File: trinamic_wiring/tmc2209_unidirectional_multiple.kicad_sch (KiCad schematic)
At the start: 3 parts

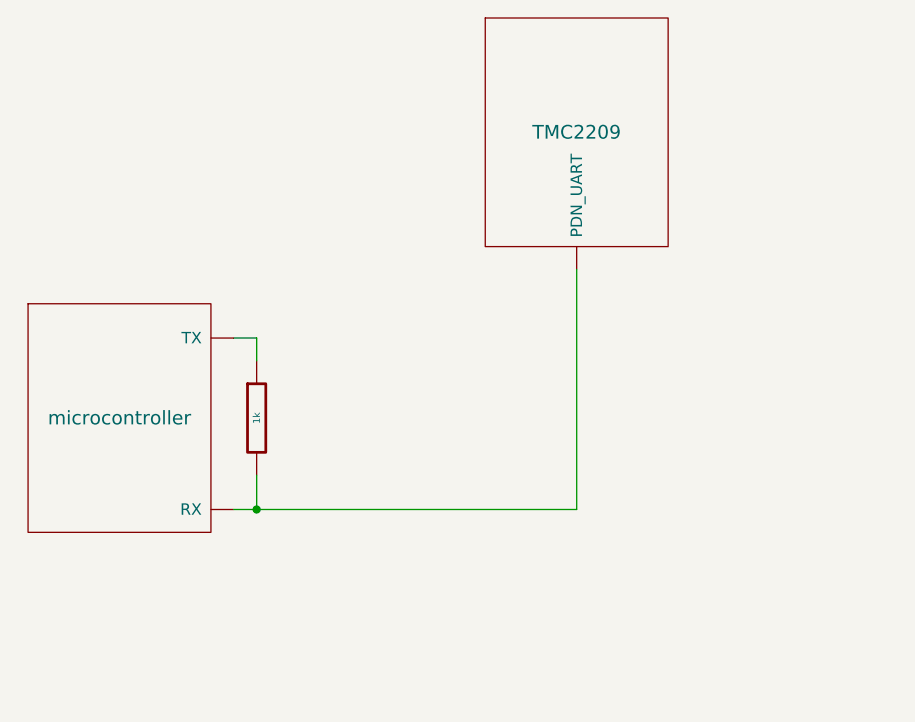
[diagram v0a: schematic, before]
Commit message: Add multiple chip schematics
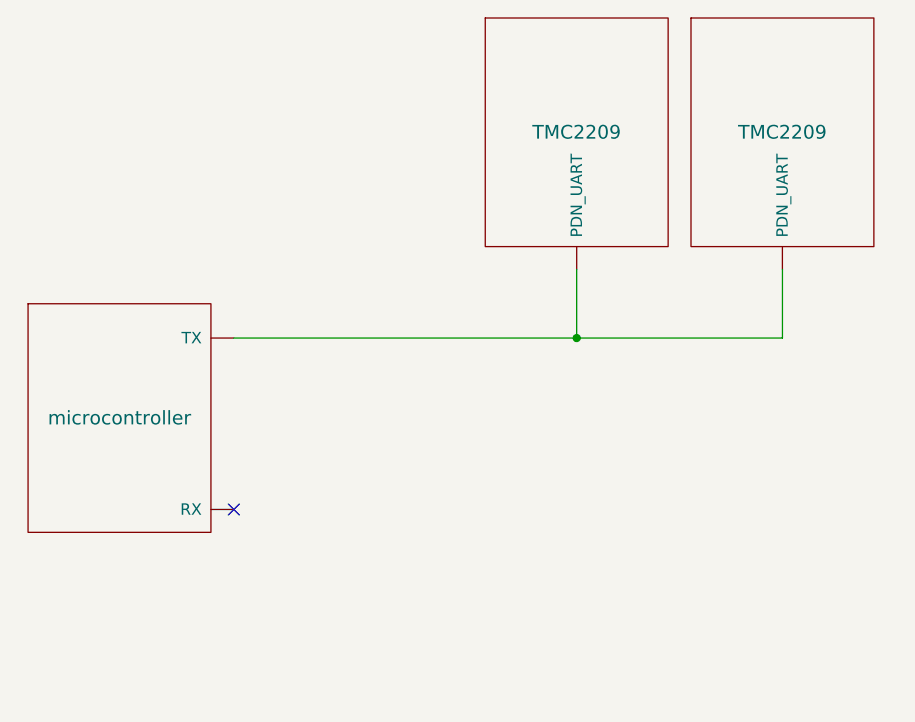
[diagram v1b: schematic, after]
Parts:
- removed R2: 1k, Janelia:R_0402_1005Metric, symbol Janelia:R_1k_0402
- added TMC?: TMC2209, symbol Janelia:SIMPLIFIED_TMC2209_UART
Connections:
- net at microcontroller?.0 (RX): no longer TMC?.0 (PDN_UART)
- net at microcontroller?.1 (TX): now also TMC?.0 (PDN_UART), TMC?.0 (PDN_UART)
- no-connect marks 0 -> 1
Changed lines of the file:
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@@
     (company "Janelia Research Campus")
   )
-  (junction (at 102.87 106.68) (diameter 0) (color 0 0 0 0)
+  (junction (at 138.43 87.63) (diameter 0) (color 0 0 0 0)
   )
-  (wire (pts (xy 102.87 87.63) (xy 102.87 90.17))
+  (no_connect (at 100.33 106.68))
+  (wire (pts (xy 138.43 87.63) (xy 161.29 87.63))
     (stroke (width 0) (type default))
   )
-  (wire (pts (xy 138.43 80.01) (xy 138.43 106.68))
+  (wire (pts (xy 138.43 80.01) (xy 138.43 87.63))
     (stroke (width 0) (type default))
   )
-  (wire (pts (xy 102.87 106.68) (xy 138.43 106.68))
+  (wire (pts (xy 100.33 87.63) (xy 138.43 87.63))
     (stroke (width 0) (type default))
   )
-  (wire (pts (xy 102.87 102.87) (xy 102.87 106.68))
-    (stroke (width 0) (type default))
-  )
-  (wire (pts (xy 100.33 87.63) (xy 102.87 87.63))
-    (stroke (width 0) (type default))
-  )
-  (wire (pts (xy 100.33 106.68) (xy 102.87 106.68))
+  (wire (pts (xy 161.29 80.01) (xy 161.29 87.63))
     (stroke (width 0) (type default))
   )
@@
           (reference "microcontroller1") (unit 1)
         )
-        (path "/e4144788-6304-493f-818e-5d881d3b7418/c8eda2b5-ab13-4033-82d9-875c9fcaf884/5f6f310d-167d-42a3-8815-1b623fe73dc8"
-          (reference "microcontroller2") (unit 1)
+        (path "/e4144788-6304-493f-818e-5d881d3b7418/c8eda2b5-ab13-4033-82d9-875c9fcaf884/5b0a2695-6b0b-4c82-b9d6-7e19fee75501"
+          (reference "microcontroller3") (unit 1)
+        )
+        (path "/e4144788-6304-493f-818e-5d881d3b7418/c8eda2b5-ab13-4033-82d9-875c9fcaf884/a2ce530e-f5b5-4e3e-9188-e4bc8f84c739"
+          (reference "microcontroller4") (unit 1)
         )
       )
@@
           (reference "TMC1") (unit 1)
         )
-        (path "/e4144788-6304-493f-818e-5d881d3b7418/c8eda2b5-ab13-4033-82d9-875c9fcaf884/5f6f310d-167d-42a3-8815-1b623fe73dc8"
-          (reference "TMC2") (unit 1)
+        (path "/e4144788-6304-493f-818e-5d881d3b7418/c8eda2b5-ab13-4033-82d9-875c9fcaf884/5b0a2695-6b0b-4c82-b9d6-7e19fee75501"
+          (reference "TMC4") (unit 1)
+        )
+        (path "/e4144788-6304-493f-818e-5d881d3b7418/c8eda2b5-ab13-4033-82d9-875c9fcaf884/a2ce530e-f5b5-4e3e-9188-e4bc8f84c739"
+          (reference "TMC6") (unit 1)
         )
       )
     )
   )
-  (symbol (lib_id "Janelia:R_1k_0402") (at 102.87 96.52 0) (unit 1)
-    (in_bom yes) (on_board yes) (dnp no)
-    (property "Reference" "R2" (at 104.14 96.52 0)
-      (effects (font (size 1.016 1.016)) (justify left) hide)
-    )
-    (property "Value" "1k" (at 102.87 96.52 90)
-      (effects (font (size 0.762 0.762)))
-    )
-    (property "Footprint" "Janelia:R_0402_1005Metric" (at 101.092 96.52 90)
-      (effects (font (size 0.762 0.762)) hide)
-    )
-    (property "Datasheet" "" (at 104.902 96.52 90)
-      (effects (font (size 0.762 0.762)))
-    )
-    (property "Vendor" "Digi-Key" (at 107.442 93.98 90)
+  (symbol (lib_id "Janelia:SIMPLIFIED_TMC2209_UART") (at 161.29 64.77 0) (unit 1)
+    (in_bom yes) (on_board yes) (dnp no) (fields_autoplaced)
+    (property "Reference" "TMC?" (at 161.29 64.77 0) (do_not_autoplace)
       (effects (font (size 1.524 1.524)) hide)
     )
-    (property "Vendor Part Number" "311-1.00KLRCT-ND" (at 109.982 91.44 90)
+    (property "Value" "TMC2209" (at 161.29 64.77 0)
+      (effects (font (size 1.524 1.524)))
+    )
+    (property "Footprint" "" (at 158.75 91.44 0)
       (effects (font (size 1.524 1.524)) hide)
     )
-    (property "Description" "RES SMD 1K OHM 1% 1/16W" (at 112.522 88.9 90)
+    (property "Datasheet" "" (at 161.29 64.77 0)
       (effects (font (size 1.524 1.524)) hide)
     )
-    (property "Package" "0402" (at 102.87 96.52 0)
-      (effects (font (size 1.27 1.27)) hide)
-    )
-    (property "Manufacturer" "YAGEO" (at 102.87 96.52 0)
-      (effects (font (size 1.27 1.27)) hide)
-    )
-    (property "Manufacturer Part Number" "RC0402FR-071KL" (at 102.87 96.52 0)
-      (effects (font (size 1.27 1.27)) hide)
-    )
-    (pin "1")
-    (pin "2")
+    (pin "0")
     (instances
       (project "trinamic_wiring"
+        (path "/e4144788-6304-493f-818e-5d881d3b7418/c8eda2b5-ab13-4033-82d9-875c9fcaf884/13e2a7b5-46df-44bb-8dde-5d79d190b8bf"
+          (reference "TMC?") (unit 1)
+        )
         (path "/e4144788-6304-493f-818e-5d881d3b7418/c8eda2b5-ab13-4033-82d9-875c9fcaf884/e3613d8e-f506-47d6-ad2d-b0f5798d9847"
-          (reference "R2") (unit 1)
+          (reference "TMC1") (unit 1)
         )
-        (path "/e4144788-6304-493f-818e-5d881d3b7418/c8eda2b5-ab13-4033-82d9-875c9fcaf884/5f6f310d-167d-42a3-8815-1b623fe73dc8"
-          (reference "R3") (unit 1)
+        (path "/e4144788-6304-493f-818e-5d881d3b7418/c8eda2b5-ab13-4033-82d9-875c9fcaf884/5b0a2695-6b0b-4c82-b9d6-7e19fee75501"
+          (reference "TMC5") (unit 1)
+        )
+        (path "/e4144788-6304-493f-818e-5d881d3b7418/c8eda2b5-ab13-4033-82d9-875c9fcaf884/a2ce530e-f5b5-4e3e-9188-e4bc8f84c739"
+          (reference "TMC7") (unit 1)
         )
       )

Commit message: Redo schematic symbols
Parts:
- removed TMC? (x2): TMC2209, symbol Janelia:SIMPLIFIED_TMC2209_UART
- removed microcontroller?: microcontroller, symbol Janelia:SIMPLIFIED_MCU_UART
- added MICROCONTROLLER4: DOC_MCU_UART, symbol Janelia:DOC_MCU_UART
- added TMC6 (x2): DOC_TMC2209, symbol Janelia:DOC_TMC2209
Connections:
- new net: MICROCONTROLLER4.1 (TX), TMC6.0 (UART), TMC6.0 (UART)
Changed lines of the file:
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@@
     (company "Janelia Research Campus")
   )
-  (junction (at 138.43 87.63) (diameter 0) (color 0 0 0 0)
+  (junction (at 148.59 77.47) (diameter 0) (color 0 0 0 0)
   )
-  (no_connect (at 100.33 106.68))
-  (wire (pts (xy 138.43 87.63) (xy 161.29 87.63))
+  (no_connect (at 125.73 97.79))
+  (wire (pts (xy 148.59 77.47) (xy 151.13 77.47))
     (stroke (width 0) (type default))
   )
-  (wire (pts (xy 138.43 80.01) (xy 138.43 87.63))
+  (wire (pts (xy 148.59 77.47) (xy 148.59 105.41))
     (stroke (width 0) (type default))
   )
-  (wire (pts (xy 100.33 87.63) (xy 138.43 87.63))
+  (wire (pts (xy 125.73 77.47) (xy 148.59 77.47))
     (stroke (width 0) (type default))
   )
-  (wire (pts (xy 161.29 80.01) (xy 161.29 87.63))
+  (wire (pts (xy 148.59 105.41) (xy 151.13 105.41))
     (stroke (width 0) (type default))
   )
-  (symbol (lib_id "Janelia:SIMPLIFIED_MCU_UART") (at 87.63 96.52 0) (unit 1)
-    (in_bom yes) (on_board yes) (dnp no)
-    (property "Reference" "microcontroller?" (at 87.63 96.52 0) (do_not_autoplace)
+  (symbol (lib_id "Janelia:DOC_MCU_UART") (at 113.03 87.63 0) (unit 1)
+    (in_bom yes) (on_board yes) (dnp no) (fields_autoplaced)
+    (property "Reference" "MICROCONTROLLER4" (at 113.03 68.58 0) (do_not_autoplace)
+      (effects (font (size 1.27 1.27)) hide)
+    )
+    (property "Value" "DOC_MCU_UART" (at 113.03 73.66 0)
       (effects (font (size 1.524 1.524)) hide)
     )
-    (property "Value" "microcontroller" (at 87.63 96.52 0)
-      (effects (font (size 1.524 1.524)))
-    )
-    (property "Footprint" "" (at 85.09 123.19 0)
+    (property "Footprint" "" (at 110.49 114.3 0)
       (effects (font (size 1.524 1.524)) hide)
     )
-    (property "Datasheet" "" (at 87.63 96.52 0)
+    (property "Datasheet" "" (at 113.03 87.63 0)
       (effects (font (size 1.524 1.524)) hide)
+    )
+    (property "Sim.Enable" "0" (at 113.03 71.12 0)
+      (effects (font (size 1.27 1.27)) hide)
     )
     (pin "0")
@@
       (project "trinamic_wiring"
         (path "/e4144788-6304-493f-818e-5d881d3b7418/c8eda2b5-ab13-4033-82d9-875c9fcaf884/13e2a7b5-46df-44bb-8dde-5d79d190b8bf"
-          (reference "microcontroller?") (unit 1)
-        )
-        (path "/e4144788-6304-493f-818e-5d881d3b7418/c8eda2b5-ab13-4033-82d9-875c9fcaf884/e3613d8e-f506-47d6-ad2d-b0f5798d9847"
-          (reference "microcontroller1") (unit 1)
+          (reference "MICROCONTROLLER4") (unit 1)
         )
         (path "/e4144788-6304-493f-818e-5d881d3b7418/c8eda2b5-ab13-4033-82d9-875c9fcaf884/5b0a2695-6b0b-4c82-b9d6-7e19fee75501"
-          (reference "microcontroller3") (unit 1)
-        )
-        (path "/e4144788-6304-493f-818e-5d881d3b7418/c8eda2b5-ab13-4033-82d9-875c9fcaf884/a2ce530e-f5b5-4e3e-9188-e4bc8f84c739"
-          (reference "microcontroller4") (unit 1)
+          (reference "MICROCONTROLLER1") (unit 1)
         )
       )
     )
   )
-  (symbol (lib_id "Janelia:SIMPLIFIED_TMC2209_UART") (at 138.43 64.77 0) (unit 1)
+  (symbol (lib_id "Janelia:DOC_TMC2209") (at 163.83 87.63 0) (unit 1)
     (in_bom yes) (on_board yes) (dnp no) (fields_autoplaced)
-    (property "Reference" "TMC?" (at 138.43 64.77 0) (do_not_autoplace)
+    (property "Reference" "TMC6" (at 163.83 68.58 0)
+      (effects (font (size 1.27 1.27)) hide)
+    )
+    (property "Value" "DOC_TMC2209" (at 163.83 73.66 0)
       (effects (font (size 1.524 1.524)) hide)
     )
-    (property "Value" "TMC2209" (at 138.43 64.77 0)
-      (effects (font (size 1.524 1.524)))
-    )
-    (property "Footprint" "" (at 135.89 91.44 0)
+    (property "Footprint" "" (at 161.29 114.3 0)
       (effects (font (size 1.524 1.524)) hide)
     )
-    (property "Datasheet" "" (at 138.43 64.77 0)
+    (property "Datasheet" "" (at 163.83 87.63 0)
       (effects (font (size 1.524 1.524)) hide)
     )
+    (property "Sim.Enable" "0" (at 163.83 71.12 0)
+      (effects (font (size 1.27 1.27)) hide)
+    )
     (pin "0")
+    (pin "1")
+    (pin "10")
+    (pin "2")
+    (pin "3")
+    (pin "4")
+    (pin "5")
+    (pin "6")
+    (pin "7")
+    (pin "8")
+    (pin "9")
     (instances
       (project "trinamic_wiring"
         (path "/e4144788-6304-493f-818e-5d881d3b7418/c8eda2b5-ab13-4033-82d9-875c9fcaf884/13e2a7b5-46df-44bb-8dde-5d79d190b8bf"
-          (reference "TMC?") (unit 1)
-        )
-        (path "/e4144788-6304-493f-818e-5d881d3b7418/c8eda2b5-ab13-4033-82d9-875c9fcaf884/e3613d8e-f506-47d6-ad2d-b0f5798d9847"
-          (reference "TMC1") (unit 1)
+          (reference "TMC6") (unit 1)
         )
         (path "/e4144788-6304-493f-818e-5d881d3b7418/c8eda2b5-ab13-4033-82d9-875c9fcaf884/5b0a2695-6b0b-4c82-b9d6-7e19fee75501"
-          (reference "TMC4") (unit 1)
-        )
-        (path "/e4144788-6304-493f-818e-5d881d3b7418/c8eda2b5-ab13-4033-82d9-875c9fcaf884/a2ce530e-f5b5-4e3e-9188-e4bc8f84c739"
-          (reference "TMC6") (unit 1)
+          (reference "TMC1") (unit 1)
         )
       )
     )
   )
-  (symbol (lib_id "Janelia:SIMPLIFIED_TMC2209_UART") (at 161.29 64.77 0) (unit 1)
+  (symbol (lib_id "Janelia:DOC_TMC2209") (at 163.83 115.57 0) (unit 1)
     (in_bom yes) (on_board yes) (dnp no) (fields_autoplaced)
-    (property "Reference" "TMC?" (at 161.29 64.77 0) (do_not_autoplace)
+    (property "Reference" "TMC6" (at 163.83 96.52 0)
+      (effects (font (size 1.27 1.27)) hide)
+    )
+    (property "Value" "DOC_TMC2209" (at 163.83 101.6 0)
       (effects (font (size 1.524 1.524)) hide)
     )
-    (property "Value" "TMC2209" (at 161.29 64.77 0)
-      (effects (font (size 1.524 1.524)))
-    )
-    (property "Footprint" "" (at 158.75 91.44 0)
+    (property "Footprint" "" (at 161.29 142.24 0)
       (effects (font (size 1.524 1.524)) hide)
     )
-    (property "Datasheet" "" (at 161.29 64.77 0)
+    (property "Datasheet" "" (at 163.83 115.57 0)
       (effects (font (size 1.524 1.524)) hide)
     )
+    (property "Sim.Enable" "0" (at 163.83 99.06 0)
+      (effects (font (size 1.27 1.27)) hide)
+    )
     (pin "0")
+    (pin "1")
+    (pin "10")
+    (pin "2")
+    (pin "3")
+    (pin "4")
+    (pin "5")
+    (pin "6")
+    (pin "7")
+    (pin "8")
+    (pin "9")
     (instances
       (project "trinamic_wiring"
         (path "/e4144788-6304-493f-818e-5d881d3b7418/c8eda2b5-ab13-4033-82d9-875c9fcaf884/13e2a7b5-46df-44bb-8dde-5d79d190b8bf"
-          (reference "TMC?") (unit 1)
-        )
-        (path "/e4144788-6304-493f-818e-5d881d3b7418/c8eda2b5-ab13-4033-82d9-875c9fcaf884/e3613d8e-f506-47d6-ad2d-b0f5798d9847"
-          (reference "TMC1") (unit 1)
+          (reference "TMC6") (unit 1)
         )
         (path "/e4144788-6304-493f-818e-5d881d3b7418/c8eda2b5-ab13-4033-82d9-875c9fcaf884/5b0a2695-6b0b-4c82-b9d6-7e19fee75501"
-          (reference "TMC5") (unit 1)
-        )
-        (path "/e4144788-6304-493f-818e-5d881d3b7418/c8eda2b5-ab13-4033-82d9-875c9fcaf884/a2ce530e-f5b5-4e3e-9188-e4bc8f84c739"
-          (reference "TMC7") (unit 1)
+          (reference "TMC8") (unit 1)
         )
       )

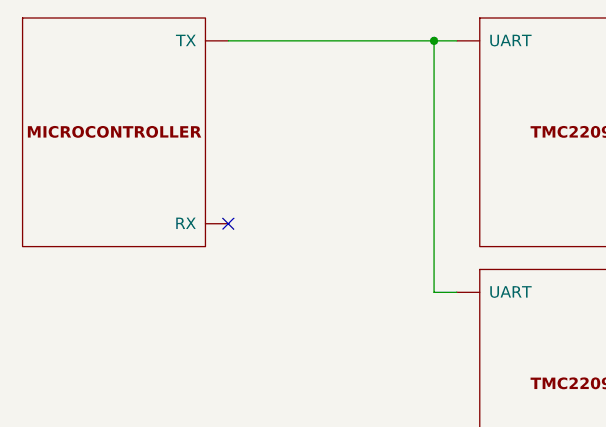
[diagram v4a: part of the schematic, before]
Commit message: Add more schematics
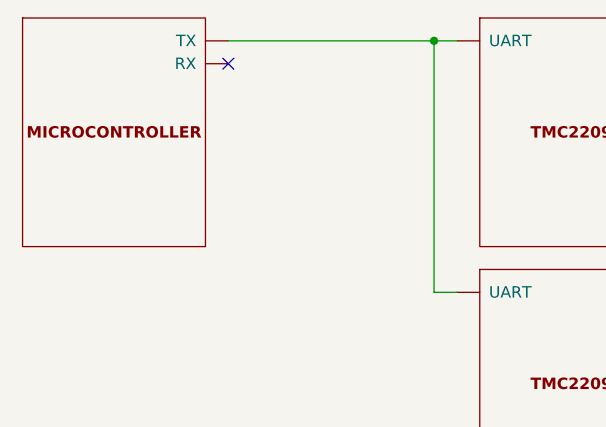
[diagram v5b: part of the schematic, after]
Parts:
- removed MICROCONTROLLER4: DOC_MCU_UART, symbol Janelia:DOC_MCU_UART
- added MICROCONTROLLER4: DOC_MCU, symbol Janelia:DOC_MCU
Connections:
- net at TMC6.0 (UART), TMC6.0 (UART): now also MICROCONTROLLER4.1 (TX)
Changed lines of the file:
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@@
   (title_block
     (title "Trinamic Wiring")
-    (date "2023-08-01")
+    (date "2023-08-02")
     (rev "0.4")
     (company "Janelia Research Campus")
@@
   (junction (at 148.59 77.47) (diameter 0) (color 0 0 0 0)
   )
-  (no_connect (at 125.73 97.79))
+  (no_connect (at 125.73 80.01))
   (wire (pts (xy 148.59 77.47) (xy 151.13 77.47))
     (stroke (width 0) (type default))
@@
     (stroke (width 0) (type default))
   )
-  (symbol (lib_id "Janelia:DOC_MCU_UART") (at 113.03 87.63 0) (unit 1)
+  (symbol (lib_id "Janelia:DOC_MCU") (at 113.03 87.63 0) (unit 1)
     (in_bom yes) (on_board yes) (dnp no) (fields_autoplaced)
-    (property "Reference" "MICROCONTROLLER4" (at 113.03 68.58 0) (do_not_autoplace)
+    (property "Reference" "MICROCONTROLLER4" (at 113.03 68.58 0)
       (effects (font (size 1.27 1.27)) hide)
     )
-    (property "Value" "DOC_MCU_UART" (at 113.03 73.66 0)
+    (property "Value" "DOC_MCU" (at 113.03 73.66 0)
       (effects (font (size 1.524 1.524)) hide)
     )
@@
     (pin "0")
     (pin "1")
+    (pin "2")
+    (pin "3")
+    (pin "4")
+    (pin "5")
+    (pin "6")
+    (pin "7")
+    (pin "8")
     (instances
       (project "trinamic_wiring"
@@
         (path "/e4144788-6304-493f-818e-5d881d3b7418/c8eda2b5-ab13-4033-82d9-875c9fcaf884/5b0a2695-6b0b-4c82-b9d6-7e19fee75501"
           (reference "MICROCONTROLLER1") (unit 1)
+        )
+        (path "/e4144788-6304-493f-818e-5d881d3b7418/c8eda2b5-ab13-4033-82d9-875c9fcaf884/d4a56977-1958-4e49-bd54-bb12e595a31d"
+          (reference "MICROCONTROLLER6") (unit 1)
         )
       )
@@
           (reference "TMC1") (unit 1)
         )
+        (path "/e4144788-6304-493f-818e-5d881d3b7418/c8eda2b5-ab13-4033-82d9-875c9fcaf884/d4a56977-1958-4e49-bd54-bb12e595a31d"
+          (reference "TMC9") (unit 1)
+        )
       )
     )
@@
           (reference "TMC8") (unit 1)
         )
+        (path "/e4144788-6304-493f-818e-5d881d3b7418/c8eda2b5-ab13-4033-82d9-875c9fcaf884/d4a56977-1958-4e49-bd54-bb12e595a31d"
+          (reference "TMC10") (unit 1)
+        )
       )
